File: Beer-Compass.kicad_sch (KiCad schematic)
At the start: 1 part, among them U1 ESP32-WROOM-32E

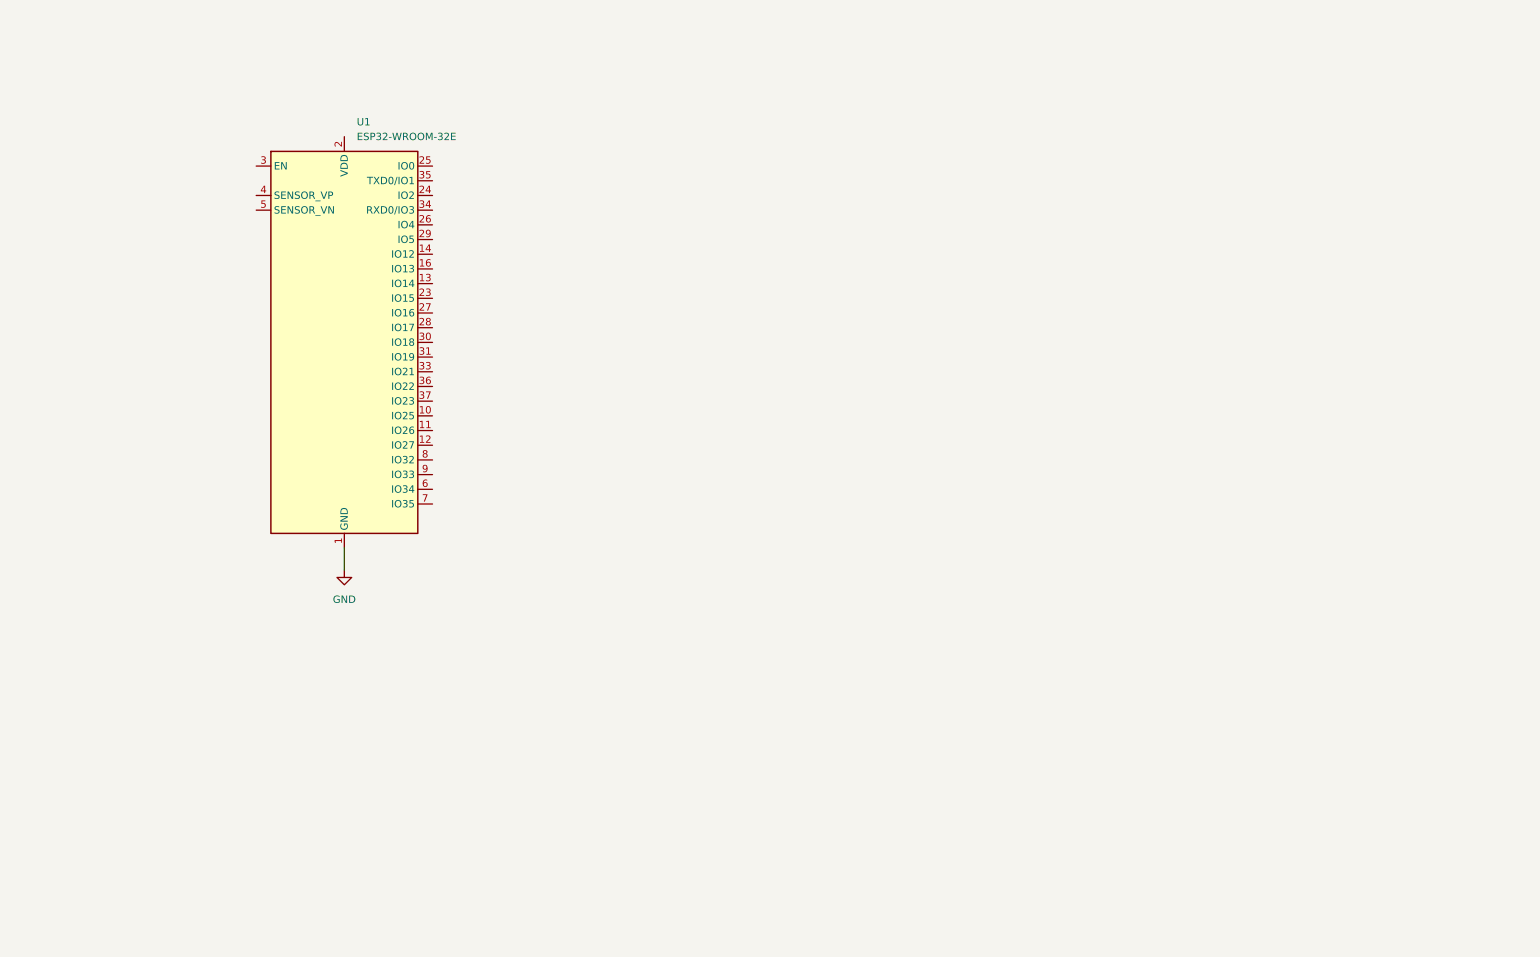
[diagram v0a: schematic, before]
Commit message: Add USB entry
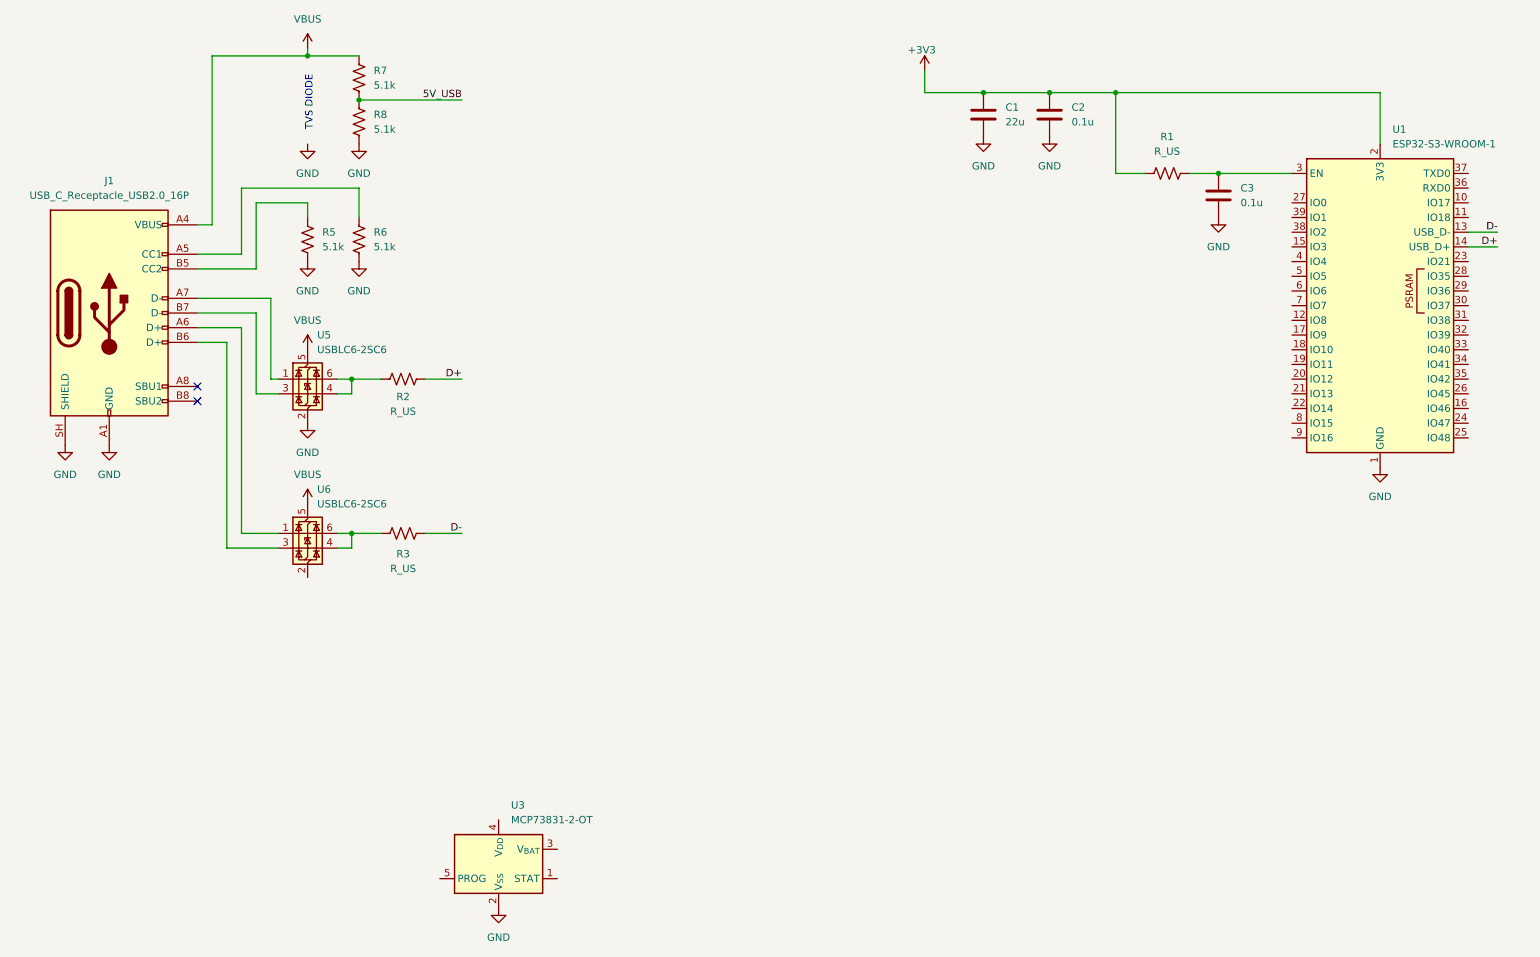
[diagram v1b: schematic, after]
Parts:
- removed U1: ESP32-WROOM-32E, RF_Module:ESP32-WROOM-32D, symbol RF_Module:ESP32-WROOM-32E
- added C1: 22u, symbol Device:C
- added C2, C3: 0.1u, symbol Device:C
- added J1: USB_C_Receptacle_USB2.0_16P, Connector_USB:USB_C_Receptacle_GCT_USB4105-xx-A_16P_TopMnt_Horizontal, symbol Connector:USB_C_Receptacle_USB2.0_16P
- added R1, R2, R3: R_US, symbol Device:R_US
- added R5, R6, R7, R8: 5.1k, symbol Device:R_US
- added U1: ESP32-S3-WROOM-1, RF_Module:ESP32-C3-DevKitM-1, symbol RF_Module:ESP32-S3-WROOM-1
- added U3: MCP73831-2-OT, Package_TO_SOT_SMD:SOT-23-5, symbol Battery_Management:MCP73831-2-OT
- added U5, U6: USBLC6-2SC6, Package_TO_SOT_SMD:SOT-23-6, symbol Power_Protection:USBLC6-2SC6
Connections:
- net GND: now also C1.2, C2.2, C3.2, J1.A1 (GND), J1.A12 (GND), J1.B1 (GND), J1.B12 (GND), J1.SH (SHIELD), R5.2, R6.2, R8.2, U1.1 (GND), U1.40 (GND), U1.41 (GND), U3.2 (V_{SS}), U5.2 (GND)
- new net: J1.A7 (D-), U5.1 (I/O1)
- new net: J1.B7 (D-), U5.3 (I/O2)
- new net: R2.1, U5.4 (I/O2), U5.6 (I/O1)
- new net: J1.A6 (D+), U6.1 (I/O1)
- new net: J1.B6 (D+), U6.3 (I/O2)
- new net: R3.1, U6.4 (I/O2), U6.6 (I/O1)
- new net: C3.1, R1.2, U1.3 (EN)
- new net: J1.A5 (CC1), R6.1
- new net: J1.B5 (CC2), R5.1
- new net +3V3: C1.1, C2.1, R1.1, U1.2 (3V3)
- new net 5V_USB: R7.2, R8.1
- new net D+: R2.2, U1.14 (USB_D+)
- new net D-: R3.2, U1.13 (USB_D-)
- new net VBUS: J1.A4 (VBUS), J1.A9 (VBUS), J1.B4 (VBUS), J1.B9 (VBUS), R7.1, U5.5 (VBUS), U6.5 (VBUS)
- no-connect marks 0 -> 2
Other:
- note added: "TVS DIODE"
